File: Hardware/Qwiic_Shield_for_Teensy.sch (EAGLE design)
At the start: 29 parts, among them J1 QWIIC_RA, J2 QWIIC_RA, J3 QWIIC_Vertical, J4 QWIIC_Vertical, J5 ALT PWR

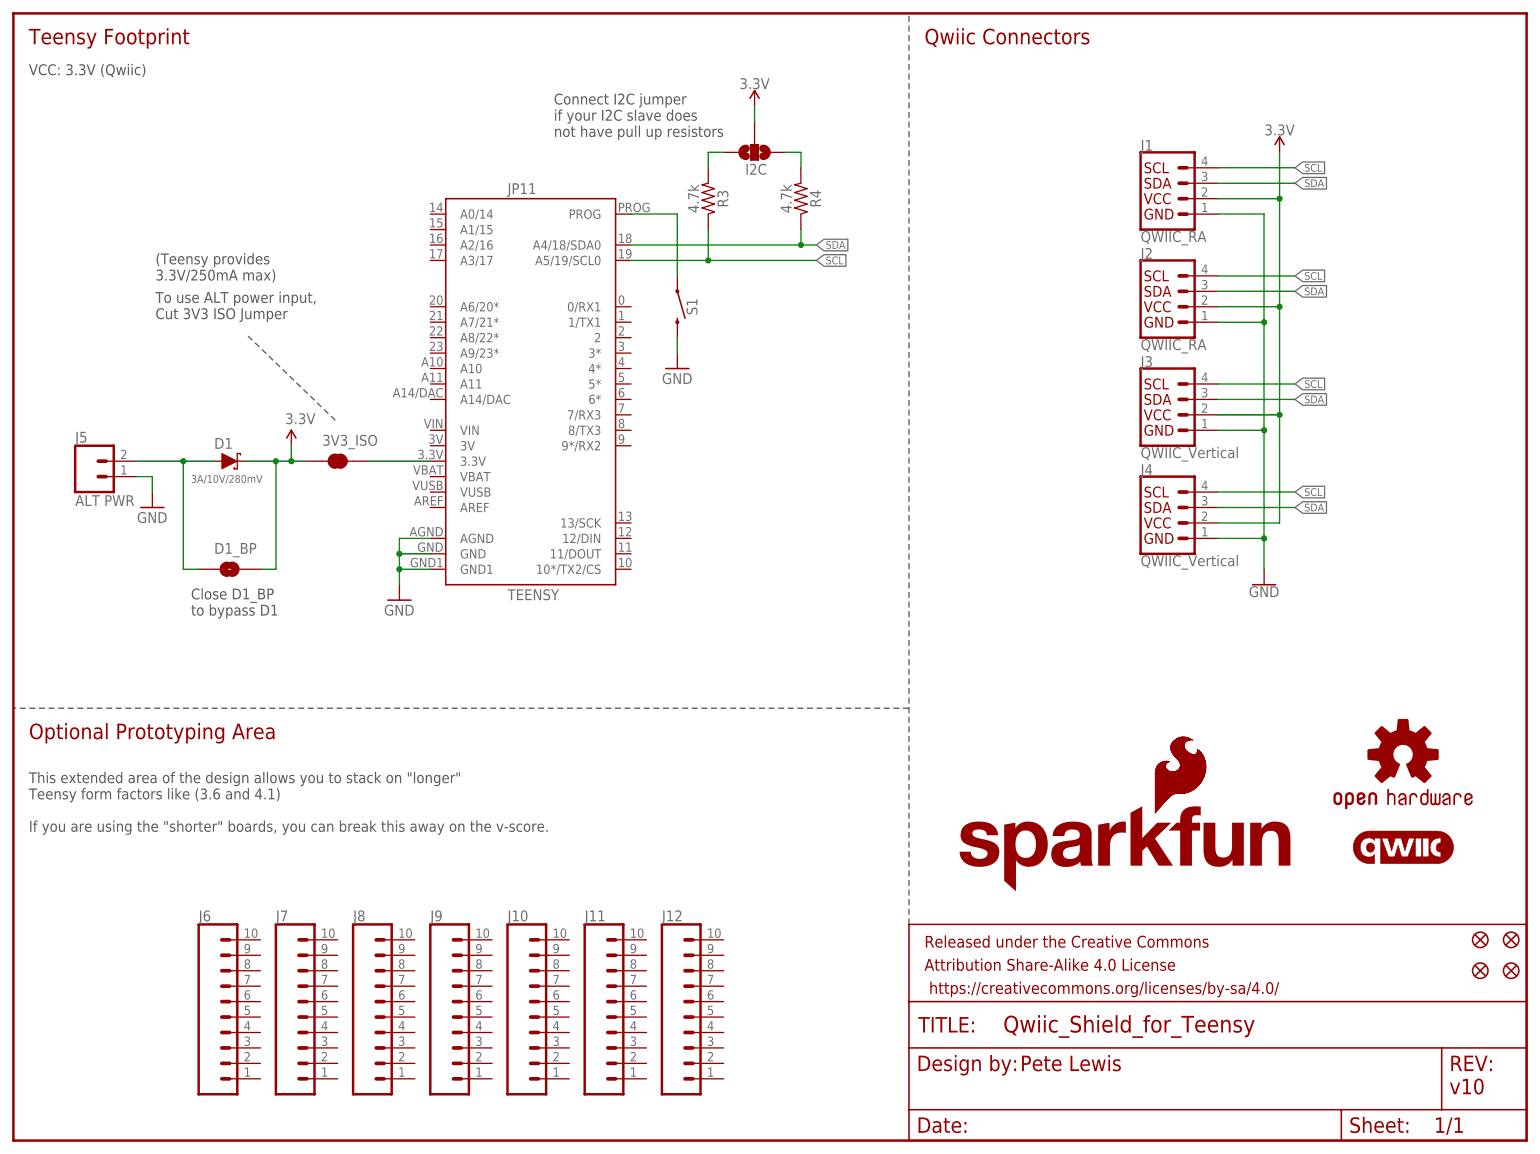
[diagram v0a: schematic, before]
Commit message: Post group review changes - short version
-"slave" terminology needs to be updated to "I2C peripheral"
-Moving to two separate products. One short and one long. Resolves the prog button access pin difference. no vscores.
-Switch up qwiic connector positions so that the north RA connector doesn't conflict with the prog button.
-3.3V power should come from the PTH header pin on the side (not the middle row).
-Added teensy qwiic shield product name to bottom silk
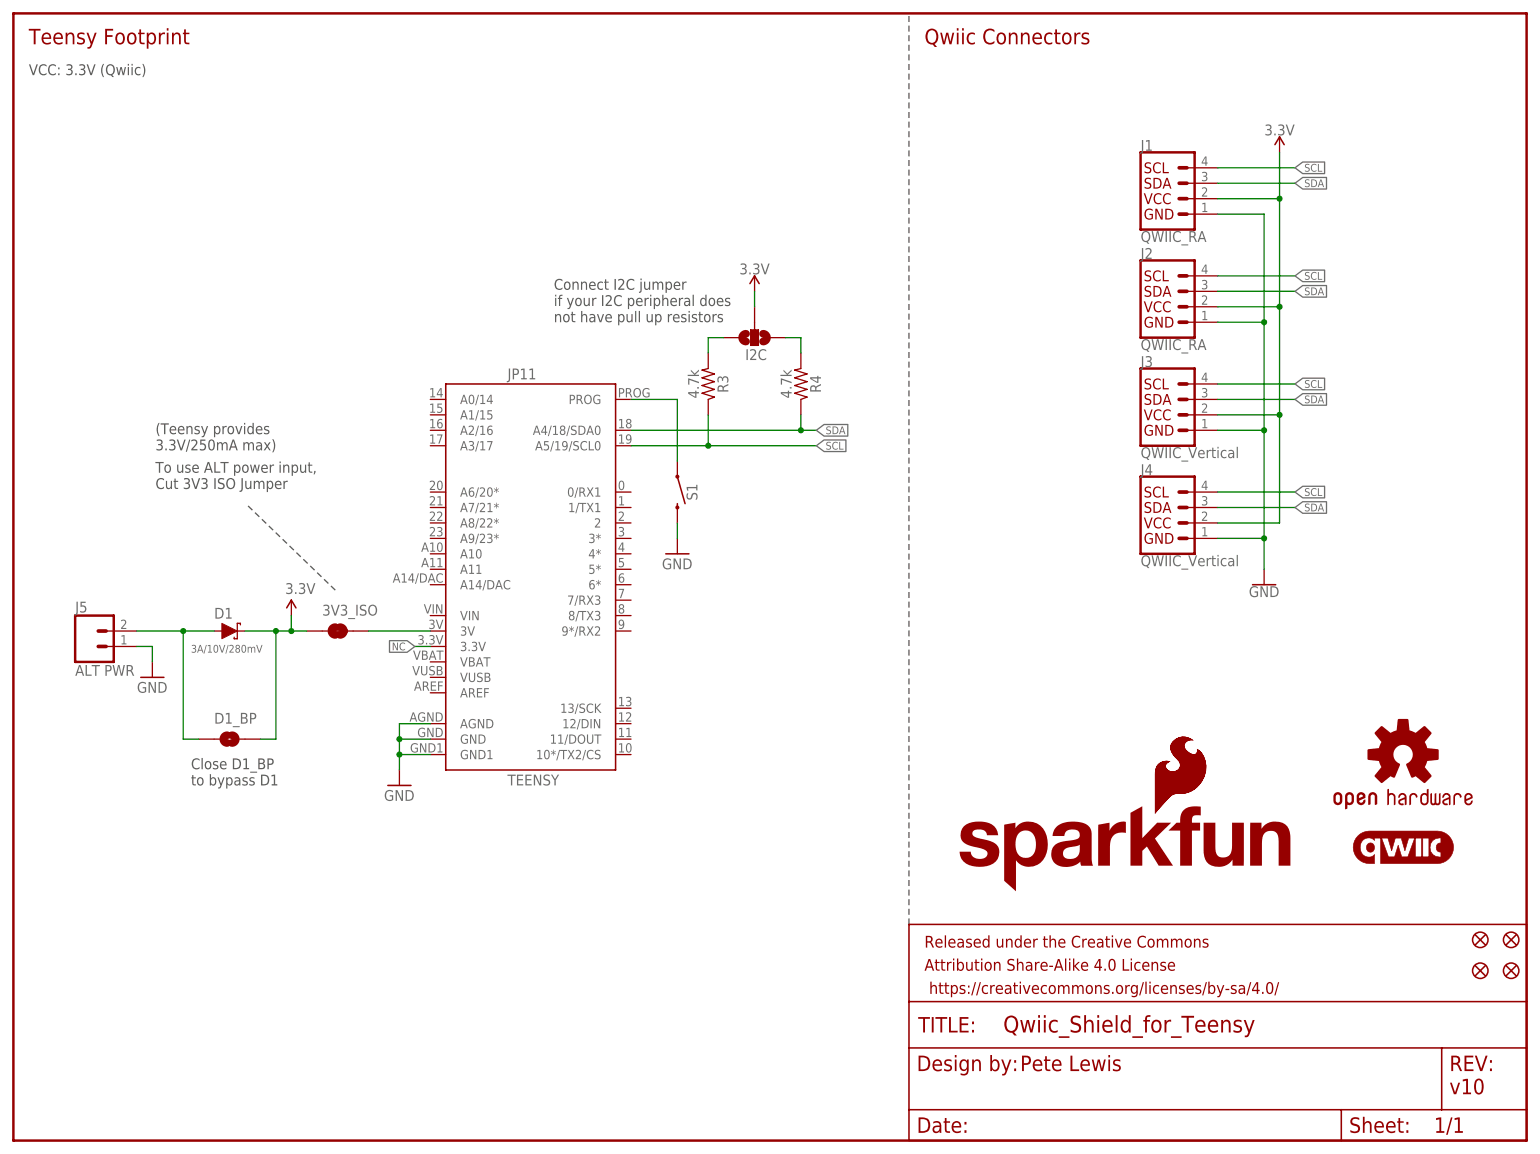
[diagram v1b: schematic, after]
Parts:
- removed J10, J11, J12, J6, J7, J8, J9: (no value), SparkFun-Connectors:CONN_10NO_SILK_PTH_FEMALE
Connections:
- new net NC: JP11.3.3V
- net N$3: now also JP11.3V; no longer JP11.3.3V
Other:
- note added: "Connect I2C jumper if your I2C peripheral does not have pull up resistors"
- note removed: "Connect I2C jumper if your I2C slave does not have pull up resistors"
- note removed: "Optional Prototyping Area"
- note removed: "This extended area of the design allows you to stack on "longer" Teensy form factors like (3.6 and 4.1) If you are using the "shorter" boards, you can break this away on the v-score."
- moved on the sheet: 3V3_ISO, D1, D1_BP, I2C, J5, JP11, R3, R4, S1

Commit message: Library updates, name prefix fix, measures update
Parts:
- removed JP11: TEENSY, SparkFun-Boards:TEENSY-3.1NOSILK
- added J6: ALT PWR, SparkFun-Connectors:CONN_021X02_NO_SILK
- J1: value QWIIC_RA -> TEENSY; device SparkFun-Connectors:QWIIC_CONNECTORJS-1MM -> teensy_boards:TEENSYNOSILK
- J3: value QWIIC_Vertical -> QWIIC_RA; device SparkFun-Connectors:QWIIC_CONNECTOR -> SparkFun-Connectors:QWIIC_CONNECTORJS-1MM
- J5: value ALT PWR -> QWIIC_Vertical; device SparkFun-Connectors:CONN_021X02_NO_SILK -> SparkFun-Connectors:QWIIC_CONNECTOR
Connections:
- net 3.3V: now also J5.2; no longer J1.2
- net GND: now also J1.AGND, J1.GND, J1.GND1, J6.1; no longer J1.1, JP11.AGND, JP11.GND, JP11.GND1
- net N$3: now also J1.3V; no longer JP11.3V
- net N$4: now also J6.2; no longer J5.2
- net N$5: now also J1.PROG; no longer JP11.PROG
- net NC: now also J1.3.3V; no longer JP11.3.3V
- net SCL: now also J1.A5/19/SCL0, J5.4; no longer J1.4, JP11.A5/19/SCL0
- net SDA: now also J1.A4/18/SDA0, J5.3; no longer J1.3, JP11.A4/18/SDA0
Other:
- moved on the sheet: J2, J3, J4

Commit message: checklist run post design review
-approved DRC overlap and clearance errors.
-one small trace nudge to remove one extra unecessary kink
-part name text adjustments for assembly sheet
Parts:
- S1: value MOMENTARY-SWITCH-SPST-SMD-5.2MM-TALL -> SMD_5.2MM
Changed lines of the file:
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@@
 <part name="D1_BP" library="SparkFun-Jumpers" deviceset="JUMPER-SMT_2_NO" device="_SILK" package3d_urn="urn:adsk.eagle:package:39279/1" value=""/>
 <part name="D1" library="SparkFun-DiscreteSemi" deviceset="DIODE-SCHOTTKY" device="-BAT60A" value="3A/10V/280mV"/>
-<part name="S1" library="SparkFun-Switches" deviceset="MOMENTARY-SWITCH-SPST" device="-SMD-5.2MM-TALL" value=""/>
+<part name="S1" library="SparkFun-Switches" deviceset="MOMENTARY-SWITCH-SPST" device="-SMD-5.2MM-TALL" value="SMD_5.2MM"/>
 <part name="GND4" library="SparkFun-Aesthetics" deviceset="GND" device=""/>
 </parts>
@@
 <instance part="S1" gate="G$1" x="109.22" y="106.68" smashed="yes" rot="R270">
 <attribute name="NAME" x="110.744" y="106.68" size="1.778" layer="95" font="vector" rot="R270" align="bottom-center"/>
-<attribute name="VALUE" x="108.712" y="106.68" size="1.778" layer="96" font="vector" rot="R270" align="top-center"/>
 </instance>
 <instance part="GND4" gate="1" x="109.22" y="96.52" smashed="yes">

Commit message: Migrating teensy part to SparkFun-Boards.lbr
-migrated teensy device from private mini library into public SparkFun-Boards.lbr
-replaced part
-deleted mini library in this repo
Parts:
- J1: device teensy_boards:TEENSYNOSILK -> SparkFun-Boards:TEENSYNOSILK
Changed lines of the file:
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@@
 <layer number="128" name="_bValues" color="7" fill="1" visible="no" active="no"/>
 <layer number="129" name="Mask" color="7" fill="1" visible="no" active="no"/>
+<layer number="130" name="SMDSTROOK" color="7" fill="1" visible="no" active="no"/>
 <layer number="131" name="tAdjust" color="7" fill="1" visible="no" active="no"/>
 <layer number="132" name="bAdjust" color="7" fill="1" visible="no" active="no"/>
+<layer number="133" name="bottom_silk" color="7" fill="1" visible="no" active="no"/>
+<layer number="134" name="silk_top" color="7" fill="1" visible="no" active="no"/>
+<layer number="135" name="silk_bottom" color="7" fill="1" visible="no" active="no"/>
+<layer number="136" name="silktop" color="7" fill="1" visible="no" active="no"/>
+<layer number="137" name="silkbottom" color="7" fill="1" visible="no" active="no"/>
+<layer number="138" name="EEE" color="7" fill="1" visible="no" active="no"/>
+<layer number="139" name="_tKeepout" color="7" fill="1" visible="no" active="no"/>
+<layer number="140" name="mbKeepout" color="7" fill="1" visible="no" active="no"/>
+<layer number="141" name="ASSEMBLY_TOP" color="7" fill="1" visible="no" active="no"/>
+<layer number="142" name="mbRestrict" color="7" fill="1" visible="no" active="no"/>
+<layer number="143" name="PLACE_BOUND_TOP" color="7" fill="1" visible="no" active="no"/>
 <layer number="144" name="Drill_legend" color="7" fill="1" visible="no" active="no"/>
+<layer number="145" name="DrillLegend_01-16" color="7" fill="1" visible="no" active="no"/>
+<layer number="146" name="DrillLegend_01-20" color="7" fill="1" visible="no" active="no"/>
+<layer number="147" name="PIN_NUMBER" color="7" fill="1" visible="no" active="no"/>
+<layer number="148" name="DrillLegend_01-20" color="7" fill="1" visible="no" active="no"/>
+<layer number="149" name="DrillLegend_02-15" color="7" fill="1" visible="no" active="no"/>
 <layer number="150" name="Notes" color="7" fill="1" visible="no" active="no"/>
 <layer number="151" name="HeatSink" color="7" fill="1" visible="no" active="no"/>
@@
 <layer number="154" name="FabDoc2" color="7" fill="1" visible="no" active="no"/>
 <layer number="155" name="FabDoc3" color="7" fill="1" visible="no" active="no"/>
+<layer number="166" name="AntennaArea" color="7" fill="1" visible="no" active="no"/>
+<layer number="168" name="4mmHeightArea" color="7" fill="1" visible="no" active="no"/>
+<layer number="191" name="mNets" color="7" fill="1" visible="no" active="no"/>
+<layer number="192" name="mBusses" color="7" fill="1" visible="no" active="no"/>
+<layer number="193" name="mPins" color="7" fill="1" visible="no" active="no"/>
+<layer number="194" name="mSymbols" color="7" fill="1" visible="no" active="no"/>
+<layer number="195" name="mNames" color="7" fill="1" visible="no" active="no"/>
+<layer number="196" name="mValues" color="7" fill="1" visible="no" active="no"/>
 <layer number="199" name="Contour" color="7" fill="1" visible="no" active="no"/>
 <layer number="200" name="200bmp" color="1" fill="10" visible="no" active="no"/>
@@
 <layer number="255" name="routoute" color="7" fill="1" visible="no" active="no"/>
 </layers>
-<schematic xreflabel="%F%N/%S.%C%R" xrefpart="/%S.%C%R">
+<schematic xreflabel="%F%N/%S" xrefpart="/%S.%C%R">
 <attributes>
 </attributes>
@@
 <part name="FD3" library="SparkFun-Aesthetics" deviceset="FIDUCIAL" device="1X2"/>
 <part name="FD4" library="SparkFun-Aesthetics" deviceset="FIDUCIAL" device="1X2"/>
-<part name="J1" library="teensy_boards" deviceset="TEENSY" device="NOSILK" value="TEENSY"/>
+<part name="J1" library="SparkFun-Boards" deviceset="TEENSY" device="NOSILK" value="TEENSY"/>
 <part name="GND3" library="SparkFun-Aesthetics" deviceset="GND" device=""/>
 <part name="SUPPLY7" library="SparkFun-Aesthetics" deviceset="3.3V" device=""/>
